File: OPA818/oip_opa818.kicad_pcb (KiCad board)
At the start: 2 copper layers, 25 x 25 mm, 32 parts, among them J101 Conn_Coaxial, J102 Conn_01x03, U101 LT3042xMSE, U102 LT3093xMSE, U103 OPA818IDRGx, U104 BUF602xDBV

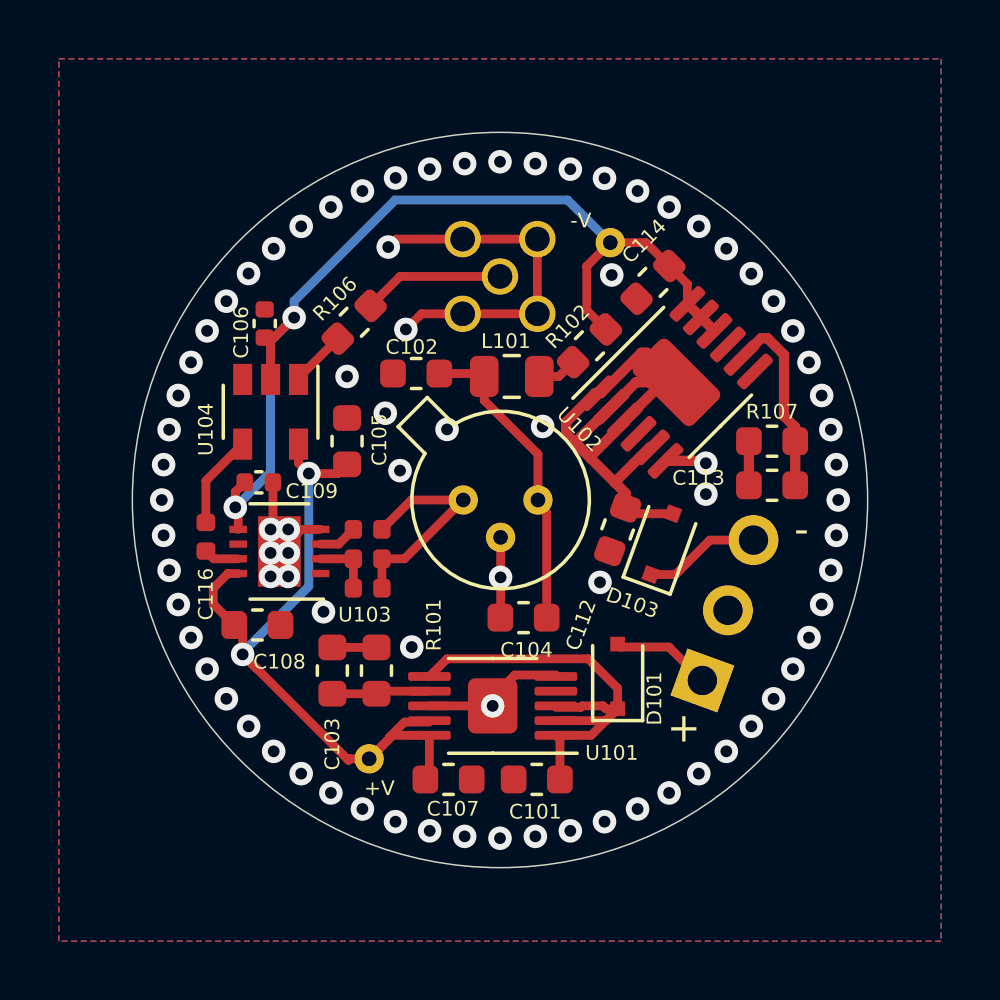
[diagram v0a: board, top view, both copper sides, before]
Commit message: dc-coupling for BUF602
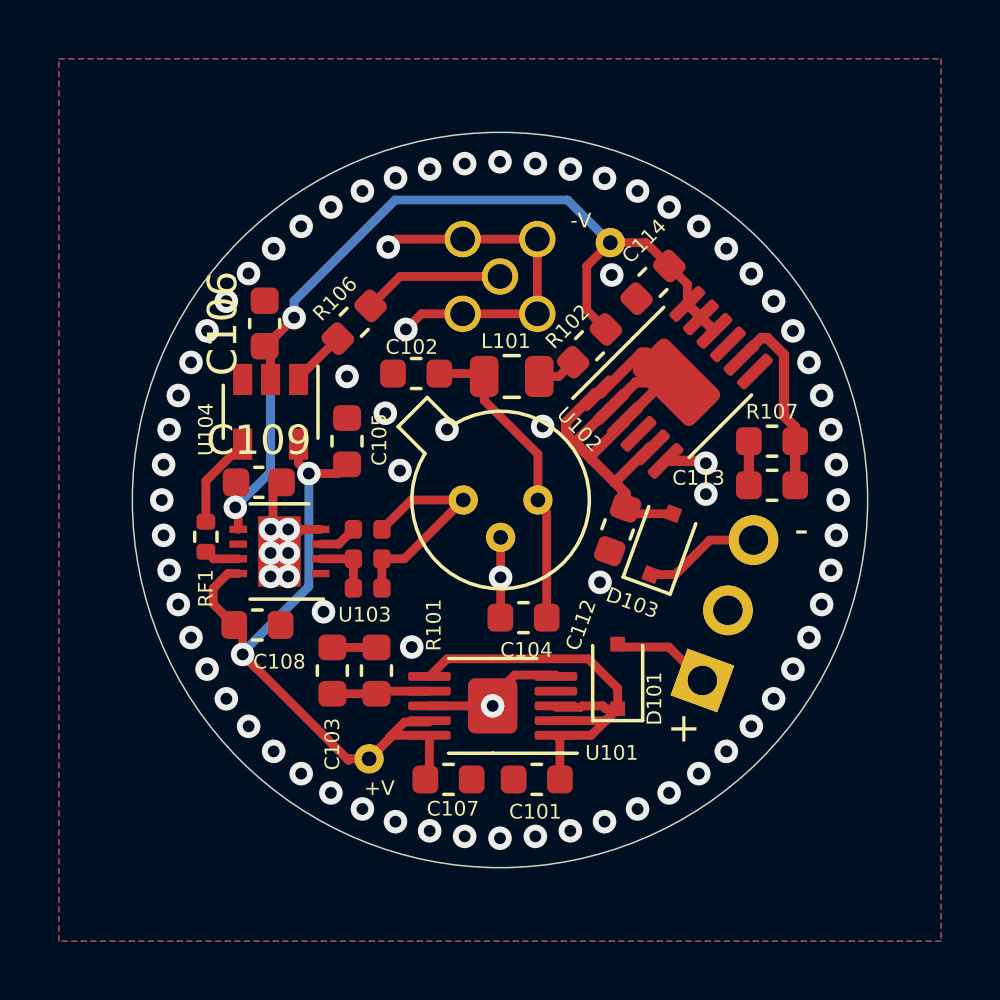
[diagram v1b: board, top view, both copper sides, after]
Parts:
- removed C116: 100n, Capacitor_SMD:C_0402_1005Metric
- added RF1: 10R, Resistor_SMD:R_0402_1005Metric, F.Cu at (140.0, 101.2)
- C106, C109: footprint Capacitor_SMD:C_0402_1005Metric -> Capacitor_SMD:C_0603_1608Metric
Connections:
- U101 pad 4: Net-(U101-Pad4) -> unconnected-(U101-Pad4)
- U102 pad 4: Net-(U102-Pad4) -> unconnected-(U102-Pad4)
- U102 pad 7: Net-(U102-Pad7) -> unconnected-(U102-Pad7)
- U103 pad 1: Net-(U103-Pad1) -> unconnected-(U103-Pad1)
- U103 pad 6: Net-(U103-Pad6) -> unconnected-(U103-Pad6)
- U104 pad 3: Net-(U104-Pad3) -> unconnected-(U104-Pad3)
